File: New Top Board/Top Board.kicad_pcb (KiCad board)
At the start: 2 copper layers, 84.9 x 67.9 mm, 35 parts, among them J1 Conn_01x04, J10 Conn_01x04, J11 Conn_01x02, J12 Conn_01x02, J13 RJE392881400, J14 RJE392881400, J2 68611514122, J3 Conn_01x06, J4 Conn_01x04, J5 Screw_Terminal_01x02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

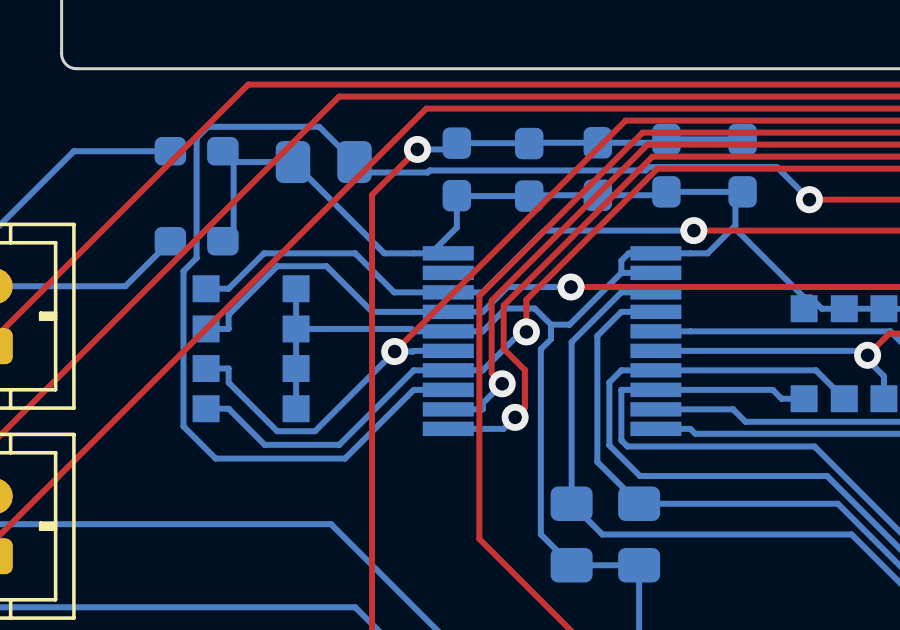
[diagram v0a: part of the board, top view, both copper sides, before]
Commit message: Corrected MC14555BDG to include a GND connection
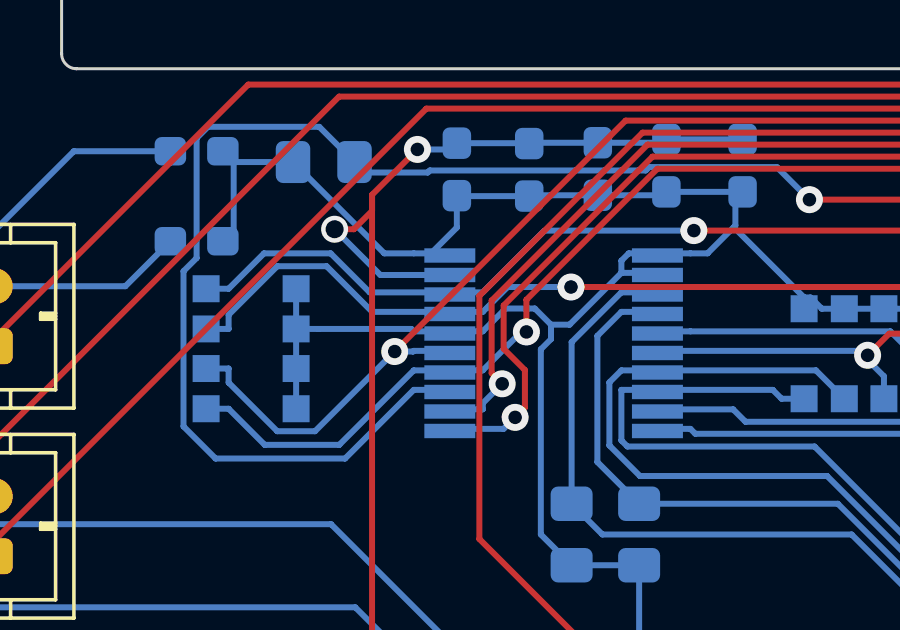
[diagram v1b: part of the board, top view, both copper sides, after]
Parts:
- moved U2 0.09 mm to (137.9, 115.9)
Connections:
- U2 pad 19: (no net) -> GND
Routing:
- net GND: track 522.1 -> 530.2 mm, vias 21 -> 22
